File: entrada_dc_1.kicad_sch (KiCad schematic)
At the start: 4 parts, among them U4 LD74-X009T, U6 74HC14

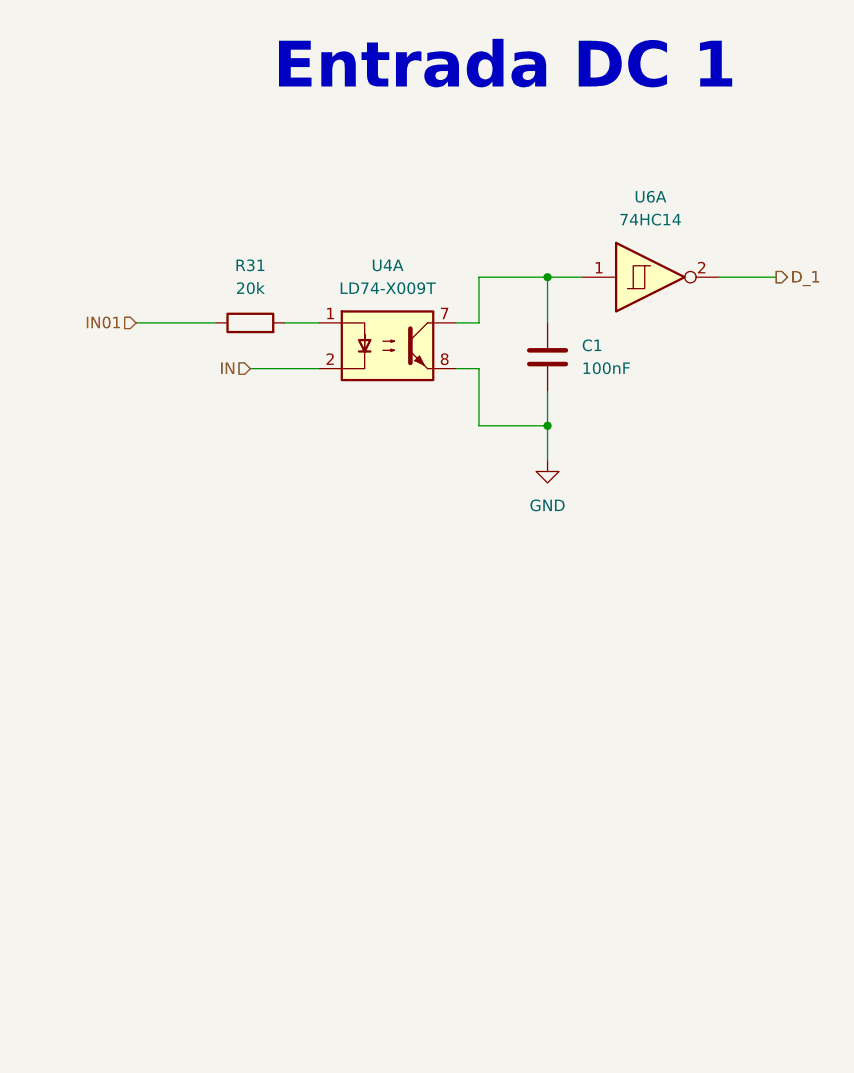
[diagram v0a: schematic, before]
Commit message: input/output separadas
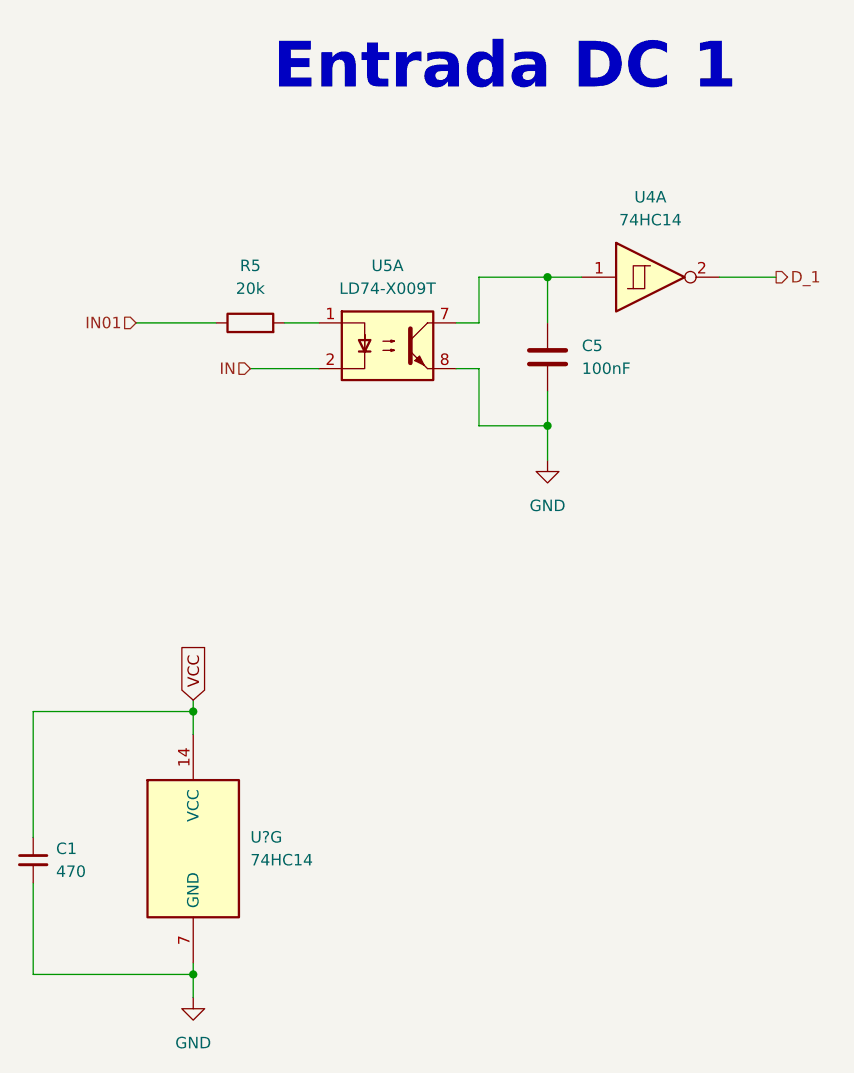
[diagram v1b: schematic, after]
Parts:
- added C1: 470, Capacitor_SMD:C_Elec_10x10.2, symbol Device:C_Small
- added U?: 74HC14, Package_SO:SOIC-14W_7.5x9mm_P1.27mm, symbol 74xx:74HC14
- renumbered C1 to C5, R31 to R5, U6 to U4, U4 to U5
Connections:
- net GND: now also C1.2, U?.7 (GND)
- new net VCC: C1.1, U?.14 (VCC)
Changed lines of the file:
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@@
   (paper "A4" portrait)
   (title_block
-    (date "2022-10-06")
+    (date "2022-10-09")
     (rev "José Luis Laica")
   )
+  (junction (at 72.39 172.72) (diameter 0) (color 0 0 0 0)
+  )
+  (junction (at 72.39 201.93) (diameter 0) (color 0 0 0 0)
+  )
   (junction (at 111.76 140.97) (diameter 0) (color 0 0 0 0)
   )
@@
     (stroke (width 0) (type default))
   )
+  (wire (pts (xy 72.39 201.93) (xy 72.39 204.47))
+    (stroke (width 0) (type default))
+  )
+  (wire (pts (xy 54.61 191.77) (xy 54.61 201.93))
+    (stroke (width 0) (type default))
+  )
+  (wire (pts (xy 54.61 186.69) (xy 54.61 172.72))
+    (stroke (width 0) (type default))
+  )
   (wire (pts (xy 111.76 144.78) (xy 111.76 140.97))
     (stroke (width 0) (type default))
@@
     (stroke (width 0) (type default))
   )
+  (wire (pts (xy 72.39 200.66) (xy 72.39 201.93))
+    (stroke (width 0) (type default))
+  )
+  (wire (pts (xy 54.61 172.72) (xy 72.39 172.72))
+    (stroke (width 0) (type default))
+  )
+  (wire (pts (xy 72.39 171.45) (xy 72.39 172.72))
+    (stroke (width 0) (type default))
+  )
+  (wire (pts (xy 72.39 172.72) (xy 72.39 175.26))
+    (stroke (width 0) (type default))
+  )
   (wire (pts (xy 104.14 129.54) (xy 104.14 124.46))
     (stroke (width 0) (type default))
@@
   )
   (wire (pts (xy 104.14 124.46) (xy 111.76 124.46))
+    (stroke (width 0) (type default))
+  )
+  (wire (pts (xy 54.61 201.93) (xy 72.39 201.93))
     (stroke (width 0) (type default))
   )
   (text "Entrada DC 1" (at 81.28 104.14 0)
     (effects (font (size 5.08 5.08) (thickness 1.016) bold) (justify left bottom))
+  )
+  (global_label "VCC" (shape input) (at 72.39 171.45 90) (fields_autoplaced)
+    (effects (font (size 1.27 1.27)) (justify left))
+    (property "Intersheet References" "${INTERSHEET_REFS}" (at 74.5808 171.45 90)
+      (effects (font (size 1.27 1.27)) (justify left))
+    )
   )
   (hierarchical_label "D_1" (shape output) (at 137.16 124.46 0) (fields_autoplaced)
@@
   (symbol (lib_id "Device:R") (at 78.74 129.54 90) (unit 1)
     (in_bom yes) (on_board yes) (dnp no) (fields_autoplaced)
-    (property "Reference" "R31" (at 78.74 123.19 90)
+    (property "Reference" "R5" (at 78.74 123.19 90)
       (effects (font (size 1.27 1.27)))
     )
@@
       (project "PLC 32 V2"
         (path "/d17a54f1-6eda-453f-95e1-42a53b02a1c3/45b8bffb-3df1-48a5-9d0c-dd39ccce2598"
-          (reference "R31") (unit 1) (value "20k") (footprint "Resistor_SMD:R_0603_1608Metric")
+          (reference "R5") (unit 1) (value "20k") (footprint "Resistor_SMD:R_0603_1608Metric")
         )
       )
@@
   (symbol (lib_id "Isolator:ILD74") (at 93.98 132.08 0) (unit 1)
     (in_bom yes) (on_board yes) (dnp no) (fields_autoplaced)
-    (property "Reference" "U4" (at 93.98 123.19 0)
+    (property "Reference" "U5" (at 93.98 123.19 0)
       (effects (font (size 1.27 1.27)))
     )
@@
       (project "PLC 32 V2"
         (path "/d17a54f1-6eda-453f-95e1-42a53b02a1c3/45b8bffb-3df1-48a5-9d0c-dd39ccce2598"
-          (reference "U4") (unit 1) (value "LD74-X009T") (footprint "Package_DIP:DIP-8_W8.89mm_SMDSocket_LongPads")
+          (reference "U5") (unit 1) (value "LD74-X009T") (footprint "Package_DIP:DIP-8_W8.89mm_SMDSocket_LongPads")
         )
       )
@@
   (symbol (lib_id "74xx:74HC14") (at 123.19 124.46 0) (unit 1)
     (in_bom yes) (on_board yes) (dnp no) (fields_autoplaced)
-    (property "Reference" "U6" (at 123.19 115.57 0)
+    (property "Reference" "U4" (at 123.19 115.57 0)
       (effects (font (size 1.27 1.27)))
     )
@@
       (project "PLC 32 V2"
         (path "/d17a54f1-6eda-453f-95e1-42a53b02a1c3/45b8bffb-3df1-48a5-9d0c-dd39ccce2598"
-          (reference "U6") (unit 1) (value "74HC14") (footprint "Package_SO:SOIC-14W_7.5x9mm_P1.27mm")
+          (reference "U4") (unit 1) (value "74HC14") (footprint "Package_SO:SOIC-14W_7.5x9mm_P1.27mm")
+        )
+      )
+    )
+  )
+  (symbol (lib_id "74xx:74HC14") (at 72.39 187.96 0) (unit 7)
+    (in_bom yes) (on_board yes) (dnp no) (fields_autoplaced)
+    (property "Reference" "U?" (at 78.74 186.6899 0)
+      (effects (font (size 1.27 1.27)) (justify left))
+    )
+    (property "Value" "74HC14" (at 78.74 189.2299 0)
+      (effects (font (size 1.27 1.27)) (justify left))
+    )
+    (property "Footprint" "Package_SO:SOIC-14W_7.5x9mm_P1.27mm" (at 72.39 187.96 0)
+      (effects (font (size 1.27 1.27)) hide)
+    )
+    (property "Datasheet" "http://www.ti.com/lit/gpn/sn74HC14" (at 72.39 187.96 0)
+      (effects (font (size 1.27 1.27)) hide)
+    )
+    (pin "1")
+    (pin "2")
+    (pin "3")
+    (pin "4")
+    (pin "5")
+    (pin "6")
+    (pin "8")
+    (pin "9")
+    (pin "10")
+    (pin "11")
+    (pin "12")
+    (pin "13")
+    (pin "14")
+    (pin "7")
+    (instances
+      (project "PLC 32 V2"
+        (path "/d17a54f1-6eda-453f-95e1-42a53b02a1c3"
+          (reference "U?") (unit 7) (value "74HC14") (footprint "Package_SO:SOIC-14W_7.5x9mm_P1.27mm")
+        )
+        (path "/d17a54f1-6eda-453f-95e1-42a53b02a1c3/45b8bffb-3df1-48a5-9d0c-dd39ccce2598"
+          (reference "U4") (unit 7) (value "74HC14") (footprint "Package_SO:SOIC-14W_7.5x9mm_P1.27mm")
         )
       )
@@
   (symbol (lib_id "power:GND") (at 111.76 144.78 0) (unit 1)
     (in_bom yes) (on_board yes) (dnp no) (fields_autoplaced)
-    (property "Reference" "#PWR017" (at 111.76 151.13 0)
+    (property "Reference" "#PWR05" (at 111.76 151.13 0)
       (effects (font (size 1.27 1.27)) hide)
     )
@@
       (project "PLC 32 V2"
         (path "/d17a54f1-6eda-453f-95e1-42a53b02a1c3/45b8bffb-3df1-48a5-9d0c-dd39ccce2598"
-          (reference "#PWR017") (unit 1) (value "GND") (footprint "")
+          (reference "#PWR05") (unit 1) (value "GND") (footprint "")
+        )
+      )
+    )
+  )
+  (symbol (lib_id "Device:C_Small") (at 54.61 189.23 0) (unit 1)
+    (in_bom yes) (on_board yes) (dnp no) (fields_autoplaced)
+    (property "Reference" "C1" (at 57.15 187.9662 0)
+      (effects (font (size 1.27 1.27)) (justify left))
+    )
+    (property "Value" "470" (at 57.15 190.5062 0)
+      (effects (font (size 1.27 1.27)) (justify left))
+    )
+    (property "Footprint" "Capacitor_SMD:C_Elec_10x10.2" (at 54.61 189.23 0)
+      (effects (font (size 1.27 1.27)) hide)
+    )
+    (property "Datasheet" "~" (at 54.61 189.23 0)
+      (effects (font (size 1.27 1.27)) hide)
+    )
+    (pin "1")
+    (pin "2")
+    (instances
+      (project "PLC 32 V2"
+        (path "/d17a54f1-6eda-453f-95e1-42a53b02a1c3/4477056d-8edb-4f95-828f-5c12bb786be6"
+          (reference "C1") (unit 1) (value "470") (footprint "Capacitor_SMD:C_Elec_10x10.2")
+        )
+        (path "/d17a54f1-6eda-453f-95e1-42a53b02a1c3"
+          (reference "C4") (unit 1) (value "470") (footprint "Capacitor_SMD:C_Elec_10x10.2")
+        )
+        (path "/d17a54f1-6eda-453f-95e1-42a53b02a1c3/45b8bffb-3df1-48a5-9d0c-dd39ccce2598"
+          (reference "C11") (unit 1) (value "470") (footprint "Capacitor_SMD:C_Elec_10x10.2")
+        )
+      )
+    )
+  )
+  (symbol (lib_id "power:GND") (at 72.39 204.47 0) (unit 1)
+    (in_bom yes) (on_board yes) (dnp no) (fields_autoplaced)
+    (property "Reference" "#PWR?" (at 72.39 210.82 0)
+      (effects (font (size 1.27 1.27)) hide)
+    )
+    (property "Value" "GND" (at 72.39 209.55 0)
+      (effects (font (size 1.27 1.27)))
+    )
+    (property "Footprint" "" (at 72.39 204.47 0)
+      (effects (font (size 1.27 1.27)) hide)
+    )
+    (property "Datasheet" "" (at 72.39 204.47 0)
+      (effects (font (size 1.27 1.27)) hide)
+    )
+    (pin "1")
+    (instances
+      (project "PLC 32 V2"
+        (path "/d17a54f1-6eda-453f-95e1-42a53b02a1c3"
+          (reference "#PWR?") (unit 1) (value "GND") (footprint "")
+        )
+        (path "/d17a54f1-6eda-453f-95e1-42a53b02a1c3/45b8bffb-3df1-48a5-9d0c-dd39ccce2598"
+          (reference "#PWR06") (unit 1) (value "GND") (footprint "")
         )
       )
@@
   (symbol (lib_id "Device:C") (at 111.76 133.35 0) (unit 1)
     (in_bom yes) (on_board yes) (dnp no) (fields_autoplaced)
-    (property "Reference" "C1" (at 115.57 132.0799 0)
+    (property "Reference" "C5" (at 115.57 132.0799 0)
       (effects (font (size 1.27 1.27)) (justify left))
     )
@@
       (project "PLC 32 V2"
         (path "/d17a54f1-6eda-453f-95e1-42a53b02a1c3/45b8bffb-3df1-48a5-9d0c-dd39ccce2598"
-          (reference "C1") (unit 1) (value "100nF") (footprint "Capacitor_SMD:C_0402_1005Metric")
-        )
-      )
+          (reference "C5") (unit 1) (value "100nF") (footprint "Capacitor_SMD:C_0402_1005Metric")
+        )
+      )

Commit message: add
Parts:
- renumbered C5 to C6, R5 to R35, U4 to U7, U5 to U8
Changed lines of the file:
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@@
   (symbol (lib_id "Device:R") (at 78.74 129.54 90) (unit 1)
     (in_bom yes) (on_board yes) (dnp no) (fields_autoplaced)
-    (property "Reference" "R5" (at 78.74 123.19 90)
+    (property "Reference" "R35" (at 78.74 123.19 90)
       (effects (font (size 1.27 1.27)))
     )
@@
       (project "PLC 32 V2"
         (path "/d17a54f1-6eda-453f-95e1-42a53b02a1c3/45b8bffb-3df1-48a5-9d0c-dd39ccce2598"
-          (reference "R5") (unit 1) (value "20k") (footprint "Resistor_SMD:R_0603_1608Metric")
+          (reference "R35") (unit 1) (value "20k") (footprint "Resistor_SMD:R_0603_1608Metric")
         )
       )
@@
   (symbol (lib_id "Isolator:ILD74") (at 93.98 132.08 0) (unit 1)
     (in_bom yes) (on_board yes) (dnp no) (fields_autoplaced)
-    (property "Reference" "U5" (at 93.98 123.19 0)
+    (property "Reference" "U8" (at 93.98 123.19 0)
       (effects (font (size 1.27 1.27)))
     )
@@
       (project "PLC 32 V2"
         (path "/d17a54f1-6eda-453f-95e1-42a53b02a1c3/45b8bffb-3df1-48a5-9d0c-dd39ccce2598"
-          (reference "U5") (unit 1) (value "LD74-X009T") (footprint "Package_DIP:DIP-8_W8.89mm_SMDSocket_LongPads")
+          (reference "U8") (unit 1) (value "LD74-X009T") (footprint "Package_DIP:DIP-8_W8.89mm_SMDSocket_LongPads")
         )
       )
@@
   (symbol (lib_id "74xx:74HC14") (at 123.19 124.46 0) (unit 1)
     (in_bom yes) (on_board yes) (dnp no) (fields_autoplaced)
-    (property "Reference" "U4" (at 123.19 115.57 0)
+    (property "Reference" "U7" (at 123.19 115.57 0)
       (effects (font (size 1.27 1.27)))
     )
@@
       (project "PLC 32 V2"
         (path "/d17a54f1-6eda-453f-95e1-42a53b02a1c3/45b8bffb-3df1-48a5-9d0c-dd39ccce2598"
-          (reference "U4") (unit 1) (value "74HC14") (footprint "Package_SO:SOIC-14W_7.5x9mm_P1.27mm")
+          (reference "U7") (unit 1) (value "74HC14") (footprint "Package_SO:SOIC-14W_7.5x9mm_P1.27mm")
         )
       )
@@
         )
         (path "/d17a54f1-6eda-453f-95e1-42a53b02a1c3/45b8bffb-3df1-48a5-9d0c-dd39ccce2598"
-          (reference "U4") (unit 7) (value "74HC14") (footprint "Package_SO:SOIC-14W_7.5x9mm_P1.27mm")
+          (reference "U7") (unit 7) (value "74HC14") (footprint "Package_SO:SOIC-14W_7.5x9mm_P1.27mm")
         )
       )
@@
         )
         (path "/d17a54f1-6eda-453f-95e1-42a53b02a1c3/45b8bffb-3df1-48a5-9d0c-dd39ccce2598"
-          (reference "C11") (unit 1) (value "470") (footprint "Capacitor_SMD:C_Elec_10x10.2")
+          (reference "C5") (unit 1) (value "470") (footprint "Capacitor_SMD:C_Elec_10x10.2")
         )
       )
@@
   (symbol (lib_id "Device:C") (at 111.76 133.35 0) (unit 1)
     (in_bom yes) (on_board yes) (dnp no) (fields_autoplaced)
-    (property "Reference" "C5" (at 115.57 132.0799 0)
+    (property "Reference" "C6" (at 115.57 132.0799 0)
       (effects (font (size 1.27 1.27)) (justify left))
     )
@@
       (project "PLC 32 V2"
         (path "/d17a54f1-6eda-453f-95e1-42a53b02a1c3/45b8bffb-3df1-48a5-9d0c-dd39ccce2598"
-          (reference "C5") (unit 1) (value "100nF") (footprint "Capacitor_SMD:C_0402_1005Metric")
-        )
-      )
+          (reference "C6") (unit 1) (value "100nF") (footprint "Capacitor_SMD:C_0402_1005Metric")
+        )
+      )
